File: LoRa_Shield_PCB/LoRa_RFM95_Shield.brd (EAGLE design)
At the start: 160 x 100 mm, 14 parts, among them J2 TYPE-C-31-M-17, U1 RFM98W, U2 3V3_REG, U3 74HC4050

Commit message: PCB artwork started
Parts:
- added JP3: (no value), pinhead_v2:1X08/OCT
- added JP4: (no value), pinhead_v2:1X06/OCT
- added JP5, JP6: (no value), pinhead_v2:1X04/OCT
- added JP7: (no value), pinhead_v2:1X01/OCT
- added SW1: (no value), special:EDG-04
- added X2: BU-SMA-H, con-coax:BU-SMA-H
- moved J2 184.3 mm to (49.8, 31.8)
- moved B2 140.3 mm to (30.5, 55.9)
- moved U3 138.5 mm to (75.9, 60.6)
- moved D1 135.9 mm to (48.3, 36.3), turned to 270 degrees
- moved C3 106.8 mm to (35.6, 76.2)
- moved C1 96.5 mm to (45.2, 36.3), turned to 270 degrees
- moved C2 77.0 mm to (36.2, 73.4)
- moved R1 74.7 mm to (29.2, 74.9)
- moved JP1 70.1 mm to (8.89, 71.1)
- moved U1 63.7 mm to (36.3, 62.7), turned to 90 degrees
- moved U2 58.1 mm to (17.3, 61.5), turned to 90 degrees
- moved LED1 54.6 mm to (29.2, 76.5), turned to 90 degrees
- moved C10 47.3 mm to (18.3, 67.1), turned to 180 degrees
- moved JP2 38.6 mm to (8.89, 47.0)
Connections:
- new net N$23: B2.3.3V, JP3.5
- new net N$24: B2.RES, JP3.6
- new net N$25: B2.IOREF, JP3.7
- new net N$26: B2.NC, JP3.8
- new net N$27: B2.A0, JP4.6
- new net N$28: B2.A1, JP4.5
- new net N$29: B2.A2, JP4.4
- new net N$30: B2.A3, JP4.3
- new net N$31: B2.A4, JP4.2
- new net N$32: B2.A5, JP4.1
- net 5V: now also B2.5V, JP3.4
- net GND: now also B2.GND@0, B2.GND@1, B2.GND@2, JP2.4, JP3.2, JP3.3, X2.2, X2.3, X2.4, X2.5
- net N$2: now also JP7.1, U1.ANT, X2.1; no longer B2.GND@0, B2.GND@1
- net N$7: now also B2.VIN, JP3.1; no longer B2.GND@2, JP2.4
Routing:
- net N$2: track 0.00 -> 10.2 mm
- added copper zone on layer 1, net GND
- added copper zone on layer 16, net GND
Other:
- board size 160 x 100 mm -> 53.6 x 59.9 mm
- board text added: "USB-C"

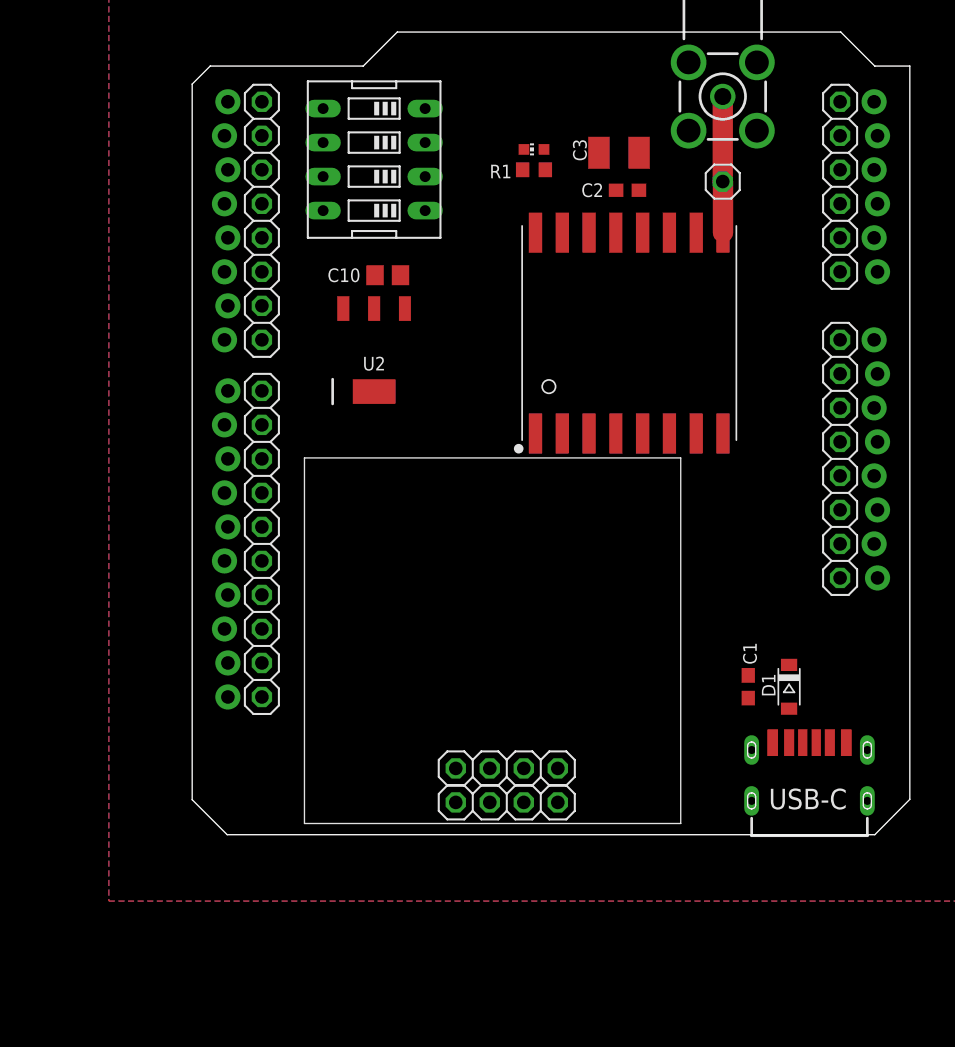
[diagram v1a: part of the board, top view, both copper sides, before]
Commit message: PCB outline
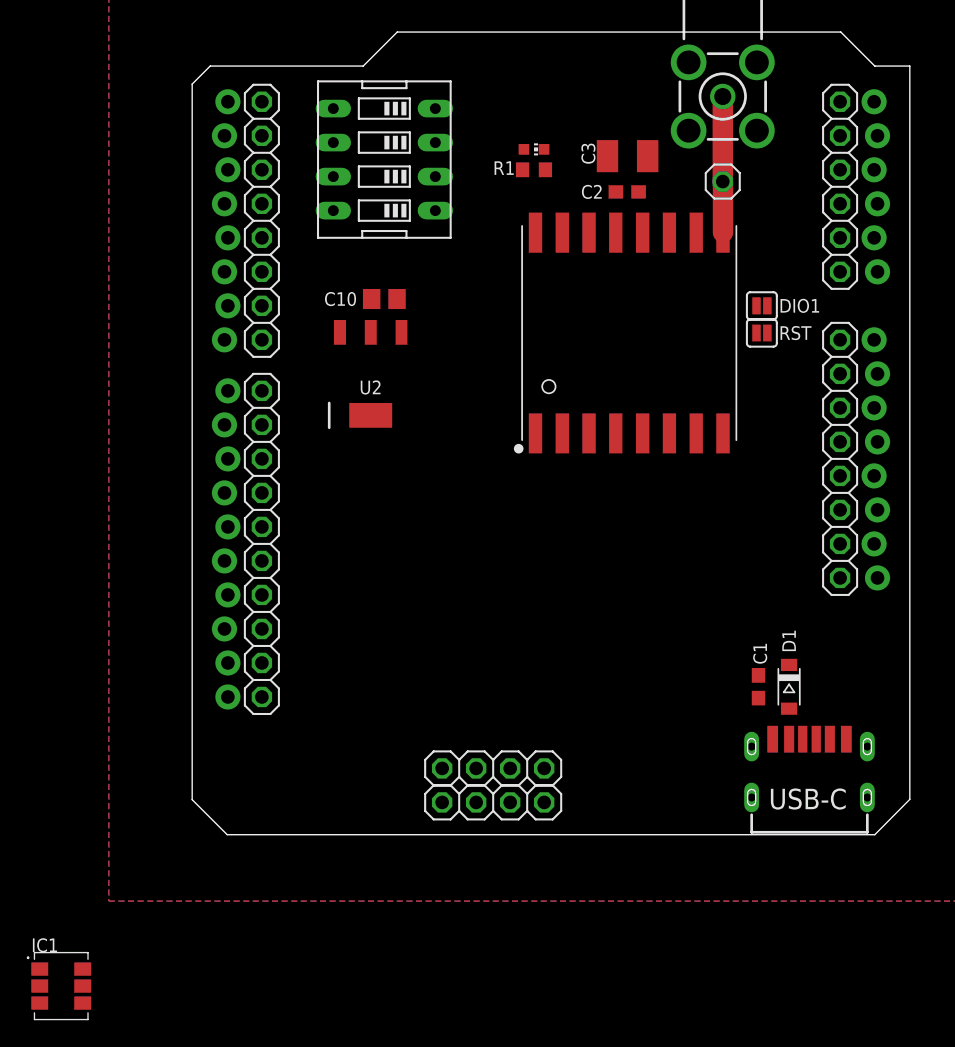
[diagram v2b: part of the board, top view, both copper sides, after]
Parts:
- added IC1: AHT10, SamacSys_Parts:AHT10
- added JP8, JP9: JUMPER-SMT_2_NO_SILK, SparkFun-Jumpers:SMT-JUMPER_2_NO_SILK
- moved U2 1.80 mm to (17.0, 59.7)
- moved C10 1.80 mm to (18.0, 65.3)
- moved JP5 1.02 mm to (26.2, 27.7)
- moved JP6 1.02 mm to (26.2, 30.2)
- moved SW1 0.76 mm to (18.0, 75.7)
- moved C1 0.76 mm to (46.0, 36.3)
- moved C3 0.68 mm to (36.2, 75.9)
- moved J2 0.25 mm to (49.8, 32.0)
- moved C2 0.13 mm to (36.2, 73.3)
- turned LED1 to 270 degrees
- turned R1 to 180 degrees
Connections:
- net N$11 renamed SPI_SS_RFM
- net N$8 renamed SPI_CLK
- removed net N$10 (its old number): B2.D11, JP2.7
- removed net N$16: B2.D5, JP1.3
- removed net N$18: B2.D3, JP1.5
- removed net N$19: B2.D2, JP1.6
- new net N$11: B2.D5, JP1.3, JP9.1
- new net RFM_DIO0: B2.D2, JP1.6, U1.DIO0
- new net RFM_DIO1: JP8.2, U1.DIO1
- new net RFM_RESET: JP9.2, U1.!RESET
- new net SPI_MISO: B2.D12, JP2.6, U1.MISO
- new net SPI_MOSI: B2.D11, JP2.7, U1.MOSI
- new net SPI_SCK: U1.SCK
- new net SPI_SS: U1.NSS
- net GND: now also SW1.5, SW1.6, SW1.7, SW1.8
- net N$27: now also SW1.4
- net N$28: now also SW1.3
- net N$29: now also SW1.2
- net N$30: now also SW1.1
- net N$9: now also B2.D3, JP1.5, JP8.1; no longer B2.D12, JP2.6
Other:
- board text added: "DIO1"
- board text added: "RST"
